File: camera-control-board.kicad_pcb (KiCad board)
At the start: 6 copper layers, 90 x 96 mm, 58 parts, among them J1 DF12NB-36DS-0.5V_51_, J2 10104110-0001LF, J3 104031-0811, J4 02x05 M 1.27mm, J5 Conn_01x09, J6 USB_C_Receptacle_USB2.0, SW1 CAS-120TA, SW3 SW_Push, U1 STM32H743IITx, U2 IS42S32800J-7TLI, U3 W25Q256JVEIQ TR, U4 XC6210B332MR, U5 WE-TVS-82400102, Y1 12MHz/7pF

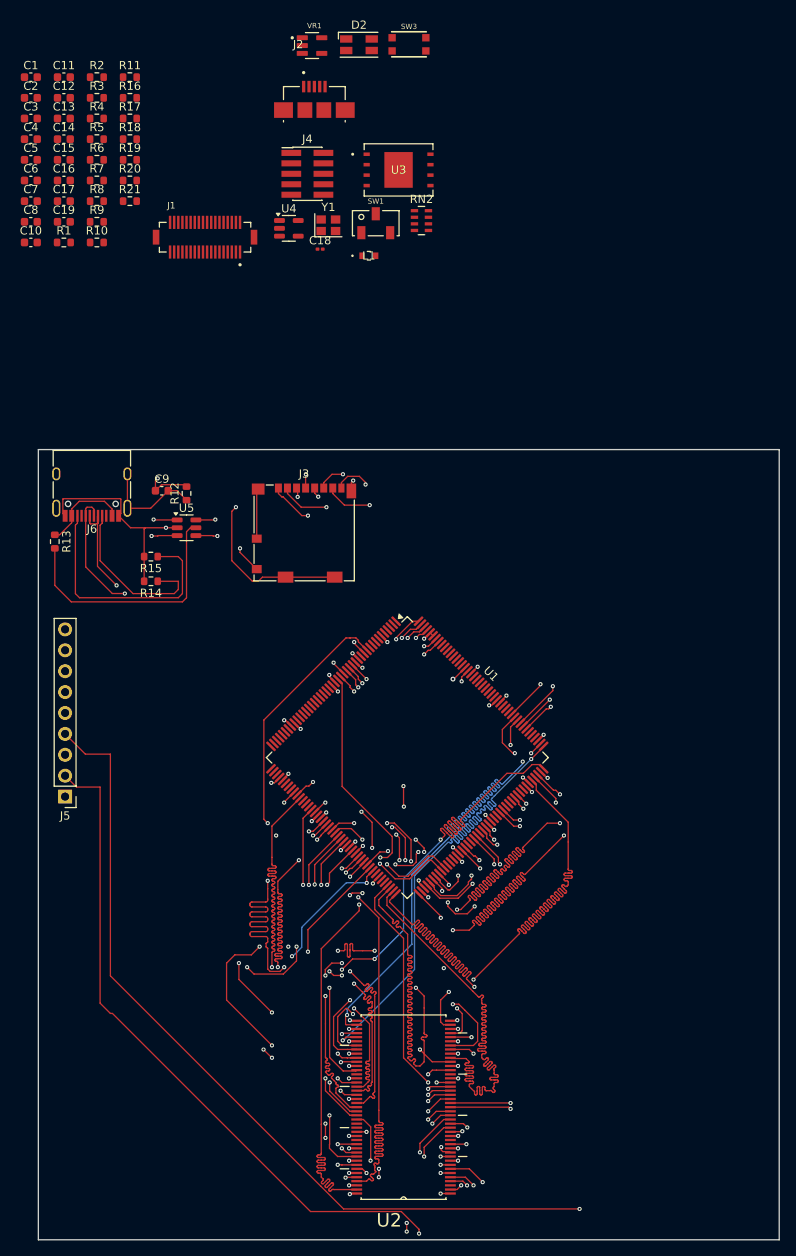
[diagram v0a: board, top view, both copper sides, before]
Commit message: image sensor routed
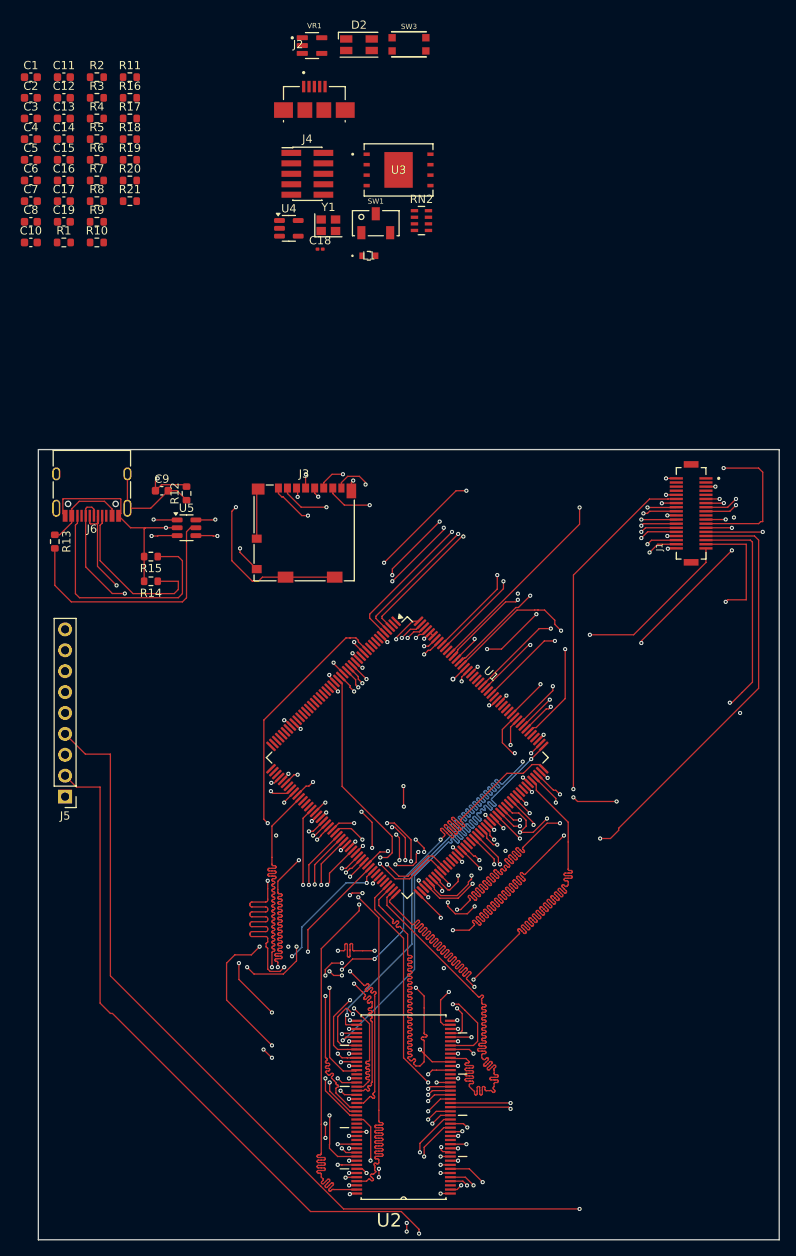
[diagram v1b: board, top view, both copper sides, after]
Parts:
- moved J1 67.9 mm to (111.8, 103.2), turned to 90 degrees
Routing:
- net /DCMI_FSIN: track 0.00 -> 122.3 mm, vias 0 -> 3
- net /DCMI_PCLK: track 0.00 -> 74.1 mm, vias 0 -> 4
- net /DCMI_HSYNC: track 0.00 -> 69.2 mm, vias 0 -> 4
- net /DCMI_D0: track 0.00 -> 68.9 mm, vias 0 -> 4
- net /DCMI_D1: track 0.00 -> 65.4 mm, vias 0 -> 2
- net /DCMI_RST: track 0.00 -> 62.7 mm, vias 0 -> 4
- net /SPI3_MOSI: track 0.00 -> 60.3 mm, vias 0 -> 4
- net /DCMI_CLK: track 0.00 -> 56.1 mm, vias 0 -> 3
- net GND: track 322.4 -> 375.8 mm, vias 30 -> 33
- net /SPI3_MISO: track 0.00 -> 53.4 mm, vias 0 -> 2
- net /DCMI_D5: track 0.00 -> 50.4 mm, vias 0 -> 2
- net /DCMI_PWDN: track 0.00 -> 48.6 mm, vias 0 -> 4
- net /SPI3_SCLK/TRACESWO: track 0.00 -> 47.0 mm, vias 0 -> 2
- net /DCMI_D7: track 0.00 -> 45.5 mm, vias 0 -> 2
- net /SPI3_SSEL: track 0.00 -> 45.3 mm, vias 0 -> 2
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
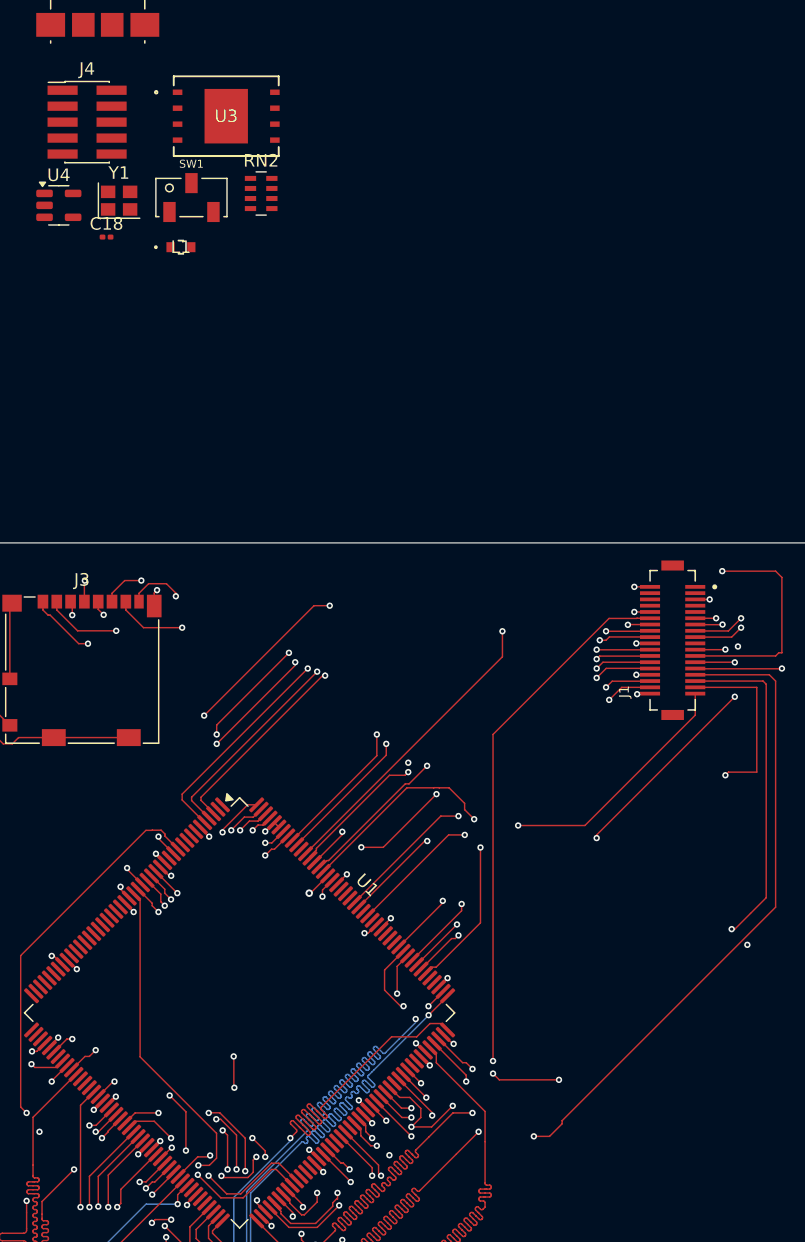
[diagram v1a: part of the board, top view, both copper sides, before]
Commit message: flash memory routed.
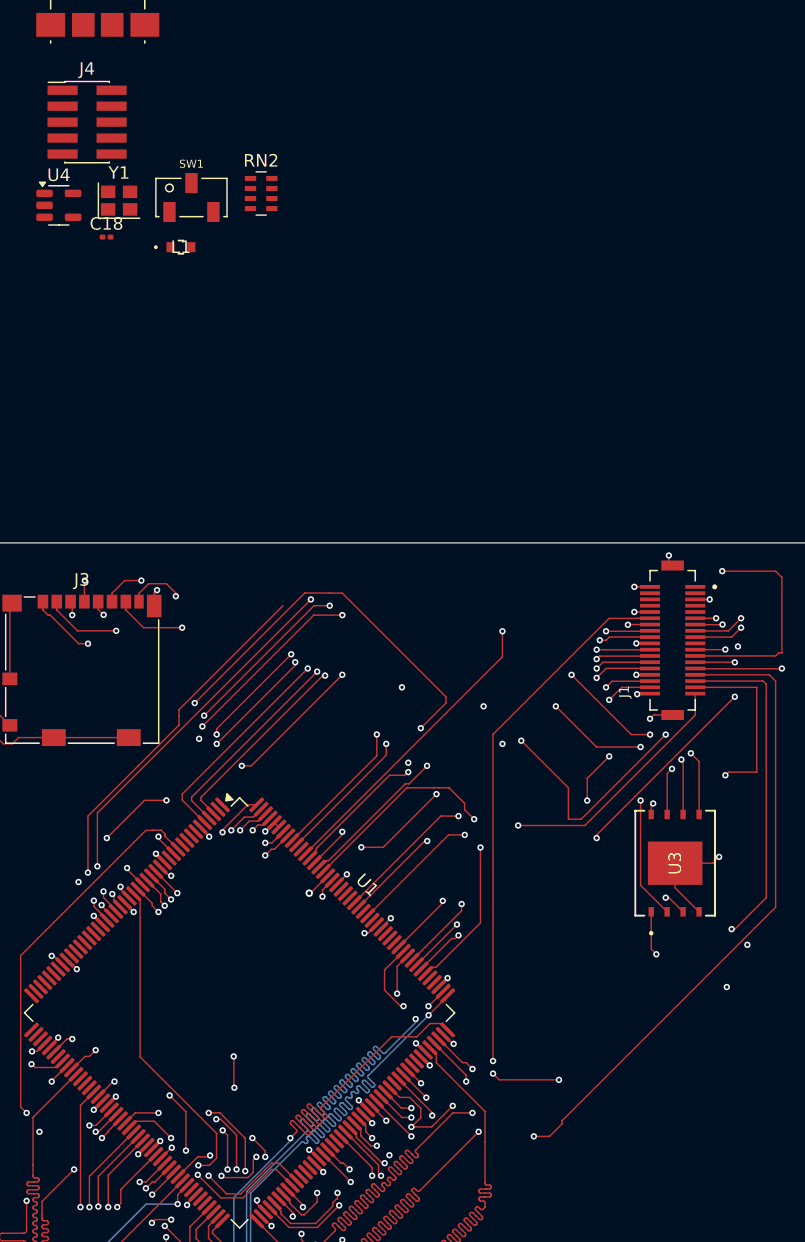
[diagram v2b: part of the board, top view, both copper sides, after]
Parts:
- moved U3 69.4 mm to (112.0, 121.0), turned to 90 degrees
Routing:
- net /FLASH_IO1: track 0.00 -> 88.4 mm, vias 0 -> 8
- net /FLASH_IO0: track 0.00 -> 75.4 mm, vias 0 -> 9
- net /FLASH_CLK: track 0.00 -> 72.5 mm, vias 0 -> 6
- net /FLASH_IO3: track 0.00 -> 70.4 mm, vias 0 -> 8
- net /FLASH_CS: track 0.00 -> 47.4 mm, vias 0 -> 3
- net /FLASH_IO2: track 0.00 -> 33.5 mm, vias 0 -> 3
- net +3.3V: track 259.8 -> 284.5 mm, vias 32 -> 33
- net GND: track 375.8 -> 396.9 mm, vias 33 -> 34
- net (no net): track 0.00 -> 16.5 mm, vias 0 -> 2

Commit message: going to update pcb from schematic (will report back)
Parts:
- removed J2: 10104110-0001LF, Argus_Connectors:AMPHENOL_10104110-0001LF
- J4, R16: moved to B.Cu
- moved SW3 120.6 mm to (36.0, 159.4)
- moved J4 86.9 mm to (112.2, 135.0)
- moved VR1 64.9 mm to (104.5, 98.5)
- moved R16 53.7 mm to (57.0, 104.8), turned to -90 degrees
- moved Y1 52.9 mm to (49.6, 118.0)
- moved D2 28.2 mm to (89.5, 68.0), turned to 90 degrees
- moved U4 24.3 mm to (53.1, 90.8)
- moved C10 23.7 mm to (54.7, 75.2)
- moved C1 16.2 mm to (47.7, 49.5), turned to 90 degrees
- moved C11 2.29 mm to (36.0, 48.0)
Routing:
- net GND: track 396.9 -> 459.0 mm, vias 34 -> 37
- net /NRST: track 0.00 -> 52.8 mm, vias 0 -> 1
- net /FLASH_IO2: track 33.5 -> 78.8 mm, vias 3 -> 7
- net +3.3V: track 284.5 -> 312.3 mm, vias 33 -> 34
- net /SWCLK: track 0.00 -> 26.1 mm, vias 0 -> 1
- net /SWDIO: track 0.00 -> 24.4 mm, vias 0 -> 1
- net /OSC_OUT: track 0.00 -> 20.3 mm, vias 0 -> 2
- net /OSC_IN: track 0.00 -> 19.3 mm, vias 0 -> 2
- net VCC: track 0.00 -> 5.36 mm
- net VDDA: track 0.00 -> 5.13 mm
- net /SD_CD: track 121.2 -> 123.1 mm

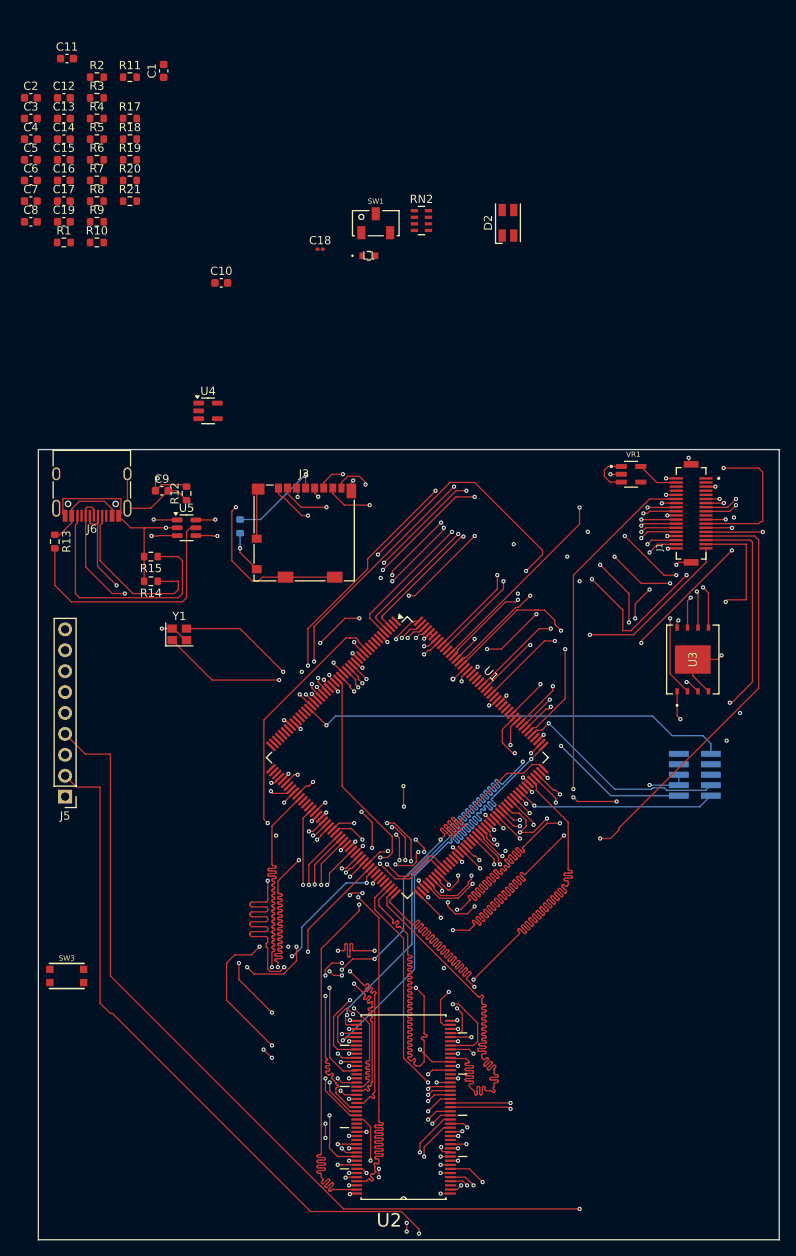
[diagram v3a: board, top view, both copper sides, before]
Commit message: Layout finished; DRC checks next.
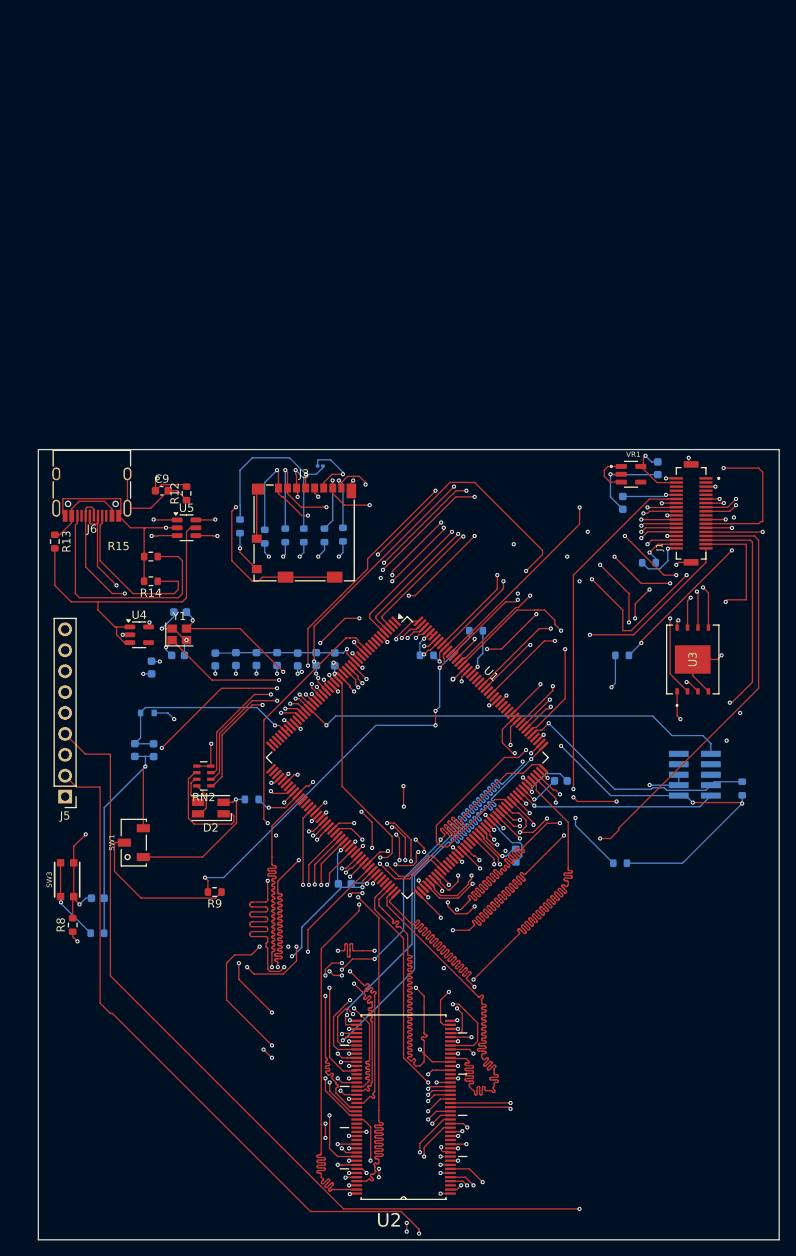
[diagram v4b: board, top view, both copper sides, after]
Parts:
- C1, C10, C11, C12, C13, C14, C15, C16, C17, C18, C19, C2, C3, C4, C5, C6, C7, C8, L1, R1, R10, R11, R17, R18, R19, R2, R20, R21, R3, R4, R5, R6, R7: moved to B.Cu
- moved R11 114.0 mm to (118.0, 136.7), turned to 90 degrees
- moved R4 99.0 mm to (39.7, 154.2)
- moved R10 98.6 mm to (103.2, 145.8)
- moved R7 96.5 mm to (90.5, 144.8), turned to 90 degrees
- moved C8 93.6 mm to (96.0, 135.8)
- moved C4 92.6 mm to (39.7, 150.0)
- moved C7 91.3 mm to (69.7, 148.2), turned to 180 degrees
- moved R8 88.0 mm to (36.7, 153.2), turned to 90 degrees
- moved R6 87.7 mm to (103.4, 120.5), turned to 180 degrees
- moved R3 87.7 mm to (106.7, 109.2)
- moved R9 82.7 mm to (53.9, 149.2), turned to 180 degrees
- moved R2 80.9 mm to (79.7, 120.5)
- moved SW1 80.8 mm to (44.1, 143.3), turned to 90 degrees
- moved D2 79.7 mm to (53.5, 139.1), turned to 180 degrees
- moved C2 77.6 mm to (68.5, 121.0), turned to -90 degrees
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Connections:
- R1 pad 1: VCC -> +3.3V
- R6 pad 2: VCC -> +3.3V
- U4 pad 1: VCC -> VBUS
- U4 pad 3: VCC -> VBUS
- VR1 pad 1: VCC -> VBUS
- VR1 pad 3: VCC -> VBUS
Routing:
- net +3.3V: track 312.3 -> 454.8 mm, vias 34 -> 48
- net GND: track 459.0 -> 564.5 mm, vias 37 -> 49
- net /BOOT0: track 0.00 -> 53.4 mm, vias 0 -> 4
- net /NRST: track 52.8 -> 102.8 mm, vias 1 -> 6
- net /VBUS_R: track 0.00 -> 49.3 mm, vias 0 -> 2
- net /VREF: track 0.00 -> 25.9 mm, vias 0 -> 1
- net /LED_B: track 0.00 -> 22.4 mm, vias 0 -> 2
- net /LED_R: track 0.00 -> 21.0 mm, vias 0 -> 2
- net Net-(SW1-B): track 0.00 -> 19.3 mm
- net /LED_G: track 0.00 -> 18.6 mm, vias 0 -> 2
- net Net-(D2-BK): track 0.00 -> 14.1 mm
- net VBUS: track 30.9 -> 44.9 mm
- net /SDIO_D2: track 48.6 -> 58.7 mm, vias 2 -> 3
- net Net-(R4-Pad1): track 0.00 -> 10.1 mm, vias 0 -> 1
- net /SDIO_CMD: track 45.2 -> 54.9 mm, vias 2 -> 3
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- added copper zone on In1.Cu, net +3.3V
- added copper zone on In4.Cu, net GND

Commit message: DRC Clean*
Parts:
- J4: moved to F.Cu
- J6: value USB_C_Receptacle_USB2.0 -> USB_C
- U5: value WE-TVS-82400102 -> WE-TVS
- moved J4 13.2 mm to (115.8, 147.8), turned to 180 degrees
- moved R2 1.71 mm to (78.0, 120.8), turned to -90 degrees
- moved C17 1.51 mm to (65.8, 119.5)
- moved C2 1.50 mm to (68.5, 119.5)
- moved C7 0.72 mm to (69.0, 148.2), turned to -90 degrees
- moved C8 0.30 mm to (96.3, 135.8)
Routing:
- net VBUS: track 44.9 -> 106.5 mm
- net GND: track 564.5 -> 609.1 mm, vias 49 -> 48
- net +3.3V: track 454.8 -> 473.4 mm, vias 48 -> 49
- net /SWCLK: track 30.1 -> 47.5 mm, vias 1 -> 2
- net (no net): track 16.5 -> 0.42 mm, vias 2 -> 0
- net /NRST: track 102.8 -> 117.7 mm, vias 6 -> 7
- net Net-(J6-SHIELD): track 12.7 -> 25.5 mm
- net /SWDIO: track 24.4 -> 36.4 mm, vias 1 -> 2
- net /I2C1_SCL: track 37.1 -> 39.4 mm
- net Net-(C7-Pad1): track 3.66 -> 5.48 mm
- net /DCMI_CLK: vias 3 -> 2
